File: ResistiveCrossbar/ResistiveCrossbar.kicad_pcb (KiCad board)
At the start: 2 copper layers, 50 x 57 mm, 10 parts, among them J1 Conn_01x07

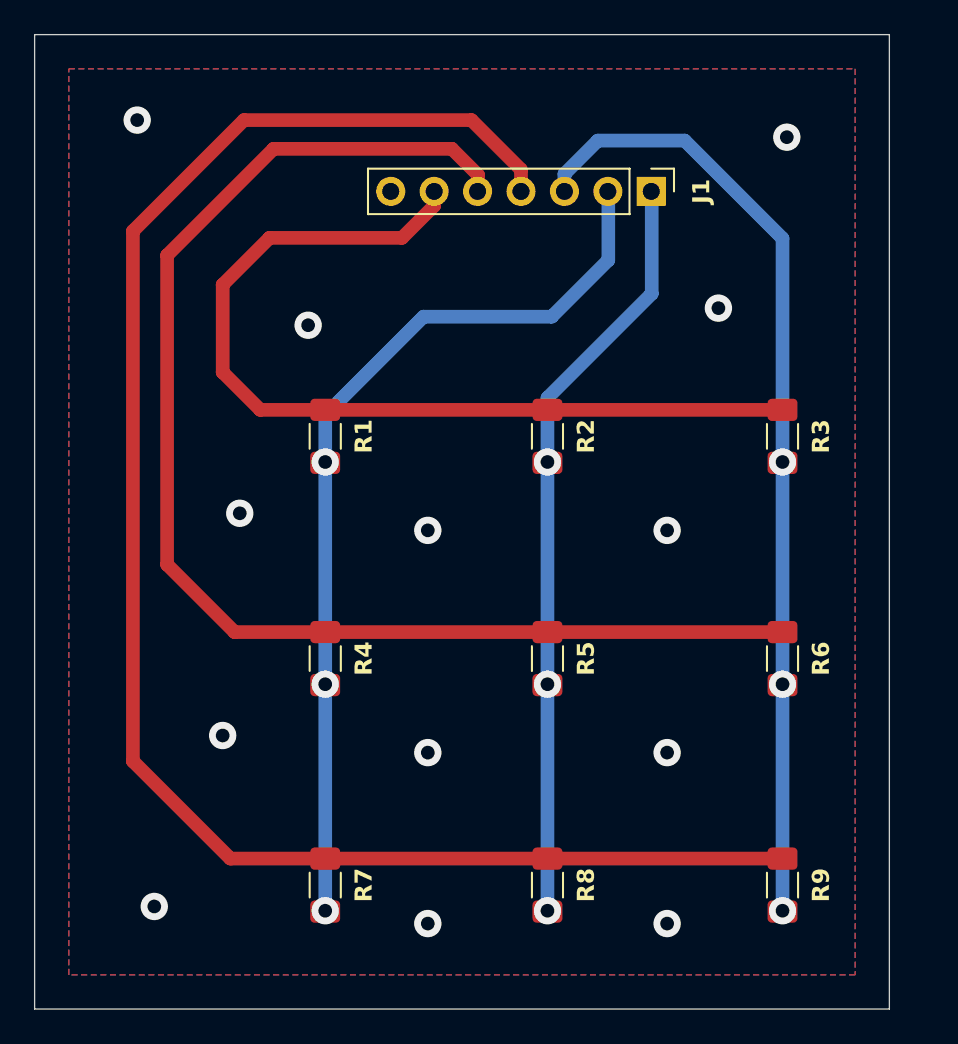
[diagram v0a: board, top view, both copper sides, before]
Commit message: Stage 2 verification done. Holes and connectors aligned. Final verification at PCB Lab left.
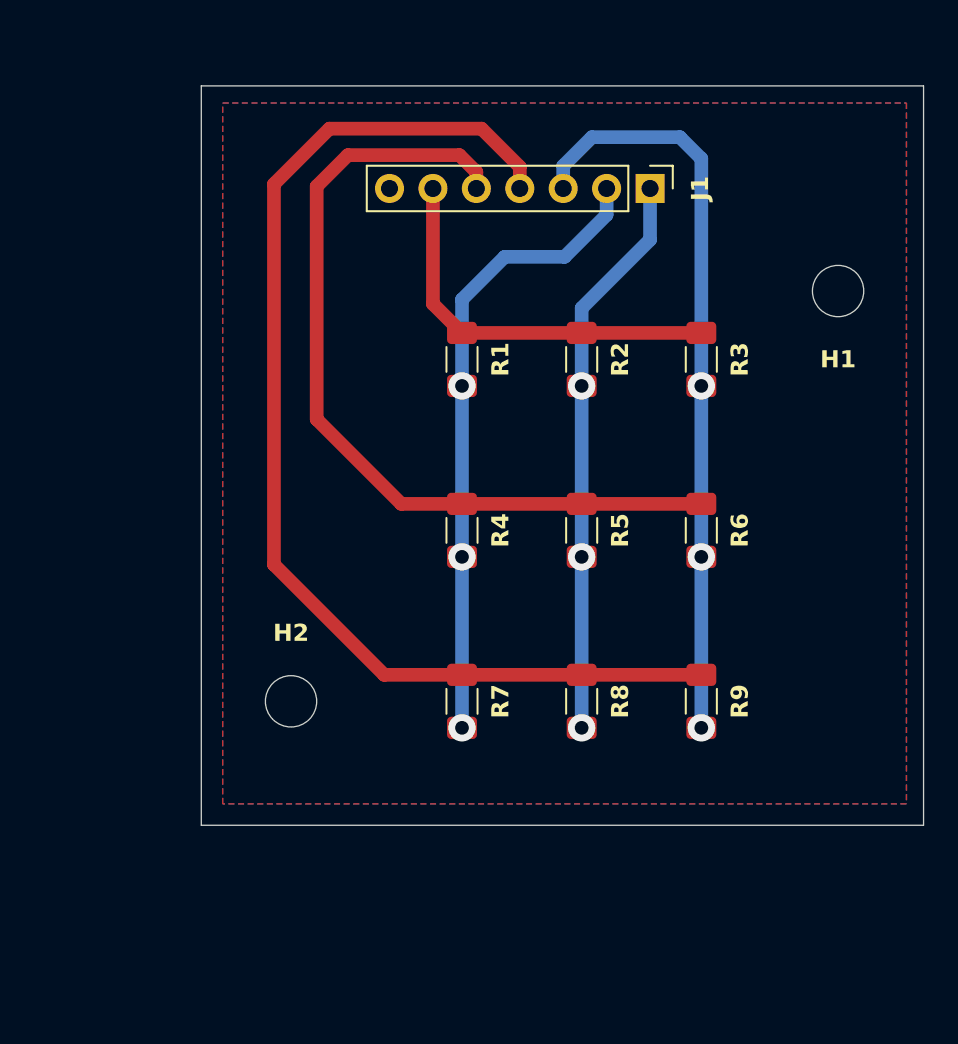
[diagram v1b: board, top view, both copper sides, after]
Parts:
- added H1: MountingHole, MountingHole:MountingHole_3mm, F.Cu at (152.0, 50.0)
- added H2: MountingHole, MountingHole:MountingHole_3mm, F.Cu at (120.0, 74.0)
- moved R7 13.4 mm to (130.0, 74.0)
- moved R9 11.8 mm to (144.0, 74.0)
- moved R4 11.0 mm to (130.0, 64.0)
- moved R8 10.9 mm to (137.0, 74.0)
- moved R1 9.18 mm to (130.0, 54.0)
- moved R6 8.88 mm to (144.0, 64.0)
- moved R5 7.76 mm to (137.0, 64.0)
- moved R3 6.54 mm to (144.0, 54.0)
- moved R2 4.92 mm to (137.0, 54.0)
- moved J1 0.19 mm to (141.0, 44.0)
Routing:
- net /Hz3: track 99.2 -> 67.8 mm
- net /Hz1: track 53.9 -> 23.2 mm
- net /Hz2: track 78.2 -> 49.6 mm
- net /Vt1: track 53.3 -> 37.1 mm
- net /Vt3: track 56.3 -> 43.9 mm
- net /Vt2: track 44.6 -> 33.2 mm
- net GND: vias 13 -> 0
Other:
- board size 50 x 57 mm -> 42.2 x 43.2 mm

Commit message: Some more alignments completed. Verification done again. Final order left.
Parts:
- J1: moved to B.Cu
- turned J1 to 90 degrees
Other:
- board text added: "3X3 Resistive Crossbar (MON-08)"

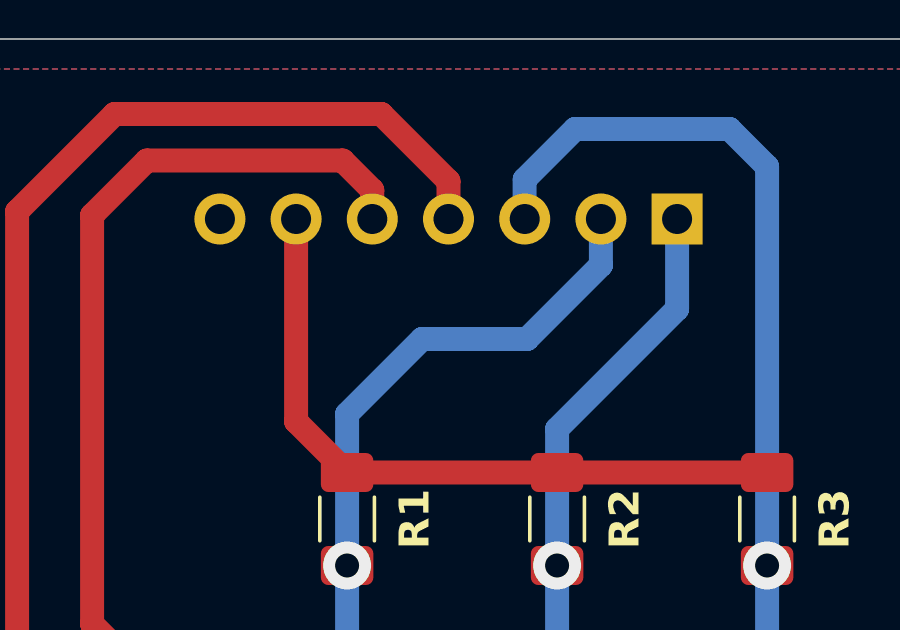
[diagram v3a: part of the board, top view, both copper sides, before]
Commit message: PCB Layout and routing of all PCBs added as per the final accepted version by the PCB Lab.
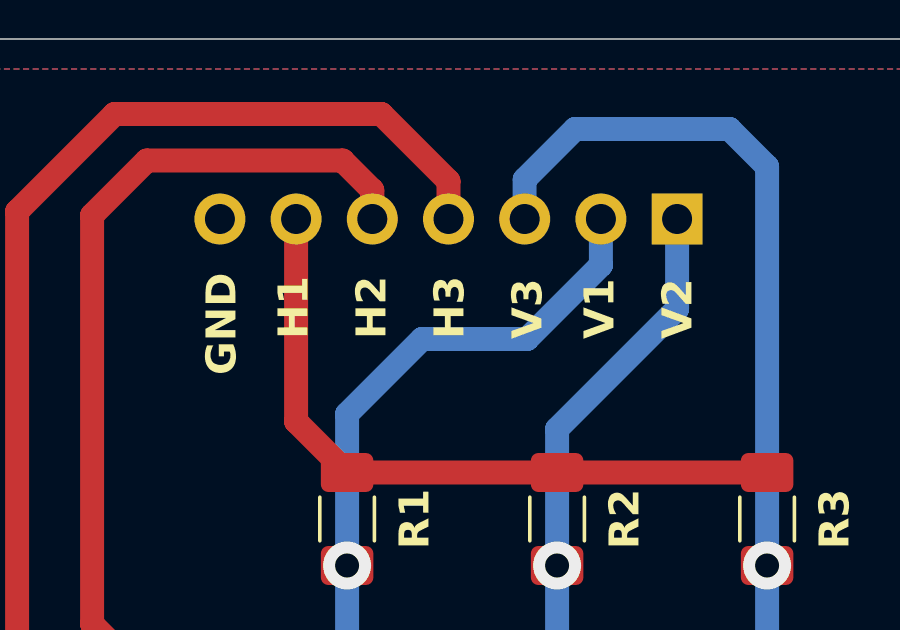
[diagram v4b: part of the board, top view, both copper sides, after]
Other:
- board text added: "GND"
- board text added: "H1"
- board text added: "H2"
- board text added: "H3"
- board text added: "V1"
- board text added: "V2"
- board text added: "V3"
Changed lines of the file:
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@@
 		(allow_soldermask_bridges_in_footprints no)
 		(pcbplotparams
-			(layerselection 0x00010fc_ffffffff)
+			(layerselection 0x0000020_7ffffffe)
 			(plot_on_all_layers_selection 0x0000000_00000000)
 			(disableapertmacros no)
@@
 			(outputformat 1)
 			(mirror no)
-			(drillshape 1)
+			(drillshape 0)
 			(scaleselection 1)
-			(outputdirectory "")
+			(outputdirectory "C:/Users/harsh/Desktop/IIT Bombay/Semester 6/EE 344/Main Work/EDL2024/ResistiveCrossbar/")
 		)
 	)
@@
 			(at 0 3 90)
 			(layer "B.SilkS")
+			(hide yes)
 			(effects
 				(font
@@
 		(layer "Edge.Cuts")
 	)
+	(gr_text "V1"
+		(at 139 48 90)
+		(layer "F.SilkS")
+		(effects
+			(font
+				(size 1 1)
+				(thickness 0.2)
+				(bold yes)
+			)
+			(justify left bottom)
+		)
+	)
+	(gr_text "H2"
+		(at 131.4 48 90)
+		(layer "F.SilkS")
+		(effects
+			(font
+				(size 1 1)
+				(thickness 0.2)
+				(bold yes)
+			)
+			(justify left bottom)
+		)
+	)
+	(gr_text "V3"
+		(at 136.6 48 90)
+		(layer "F.SilkS")
+		(effects
+			(font
+				(size 1 1)
+				(thickness 0.2)
+				(bold yes)
+			)
+			(justify left bottom)
+		)
+	)
+	(gr_text "H1"
+		(at 128.8 48 90)
+		(layer "F.SilkS")
+		(effects
+			(font
+				(size 1 1)
+				(thickness 0.2)
+				(bold yes)
+			)
+			(justify left bottom)
+		)
+	)
+	(gr_text "V2"
+		(at 141.6 48 90)
+		(layer "F.SilkS")
+		(effects
+			(font
+				(size 1 1)
+				(thickness 0.2)
+				(bold yes)
+			)
+			(justify left bottom)
+		)
+	)
 	(gr_text "3X3\nResistive\nCrossbar\n(MON-08)"
 		(at 147 72 0)
@@
 		)
 	)
+	(gr_text "GND"
+		(at 126.4 49.2 90)
+		(layer "F.SilkS")
+		(effects
+			(font
+				(size 1 1)
+				(thickness 0.2)
+				(bold yes)
+			)
+			(justify left bottom)
+		)
+	)
+	(gr_text "H3"
+		(at 134 48 90)
+		(layer "F.SilkS")
+		(effects
+			(font
+				(size 1 1)
+				(thickness 0.2)
+				(bold yes)
+			)
+			(justify left bottom)
+		)
+	)
+	(dimension
+		(type aligned)
+		(layer "Dwgs.User")
+		(pts
+			(xy 114.75 81.25) (xy 157 81.25)
+		)
+		(height 3.15)
+		(gr_text "42.2500 mm"
+			(at 135.875 83.25 0)
+			(layer "Dwgs.User")
+			(effects
+				(font
+					(size 1 1)
+					(thickness 0.15)
+				)
+			)
+		)
+		(format
+			(prefix "")
+			(suffix "")
+			(units 3)
+			(units_format 1)
+			(precision 4)
+		)
+		(style
+			(thickness 0.1)
+			(arrow_length 1.27)
+			(text_position_mode 0)
+			(extension_height 0.58642)
+			(extension_offset 0.5) keep_text_aligned)
+	)
+	(dimension
+		(type aligned)
+		(layer "Dwgs.User")
+		(pts
+			(xy 157 38) (xy 157 81.25)
+		)
+		(height -2.8)
+		(gr_text "43.2500 mm"
+			(at 158.65 59.625 90)
+			(layer "Dwgs.User")
+			(effects
+				(font
+					(size 1 1)
+					(thickness 0.15)
+				)
+			)
+		)
+		(format
+			(prefix "")
+			(suffix "")
+			(units 3)
+			(units_format 1)
+			(precision 4)
+		)
+		(style
+			(thickness 0.1)
+			(arrow_length 1.27)
+			(text_position_mode 0)
+			(extension_height 0.58642)
+			(extension_offset 0.5) keep_text_aligned)
+	)
 	(via
